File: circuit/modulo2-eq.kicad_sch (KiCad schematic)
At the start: 63 parts, among them J1 JACK_MONO, J2 HOLE, J3 HOLE, J4 CONN_01X04, J5 CONN_01X02, Q1 MMBFJ201, U1 NE5532, U2 NE5532, U3 NE5532, U4 NE5532, U5 TLE2426

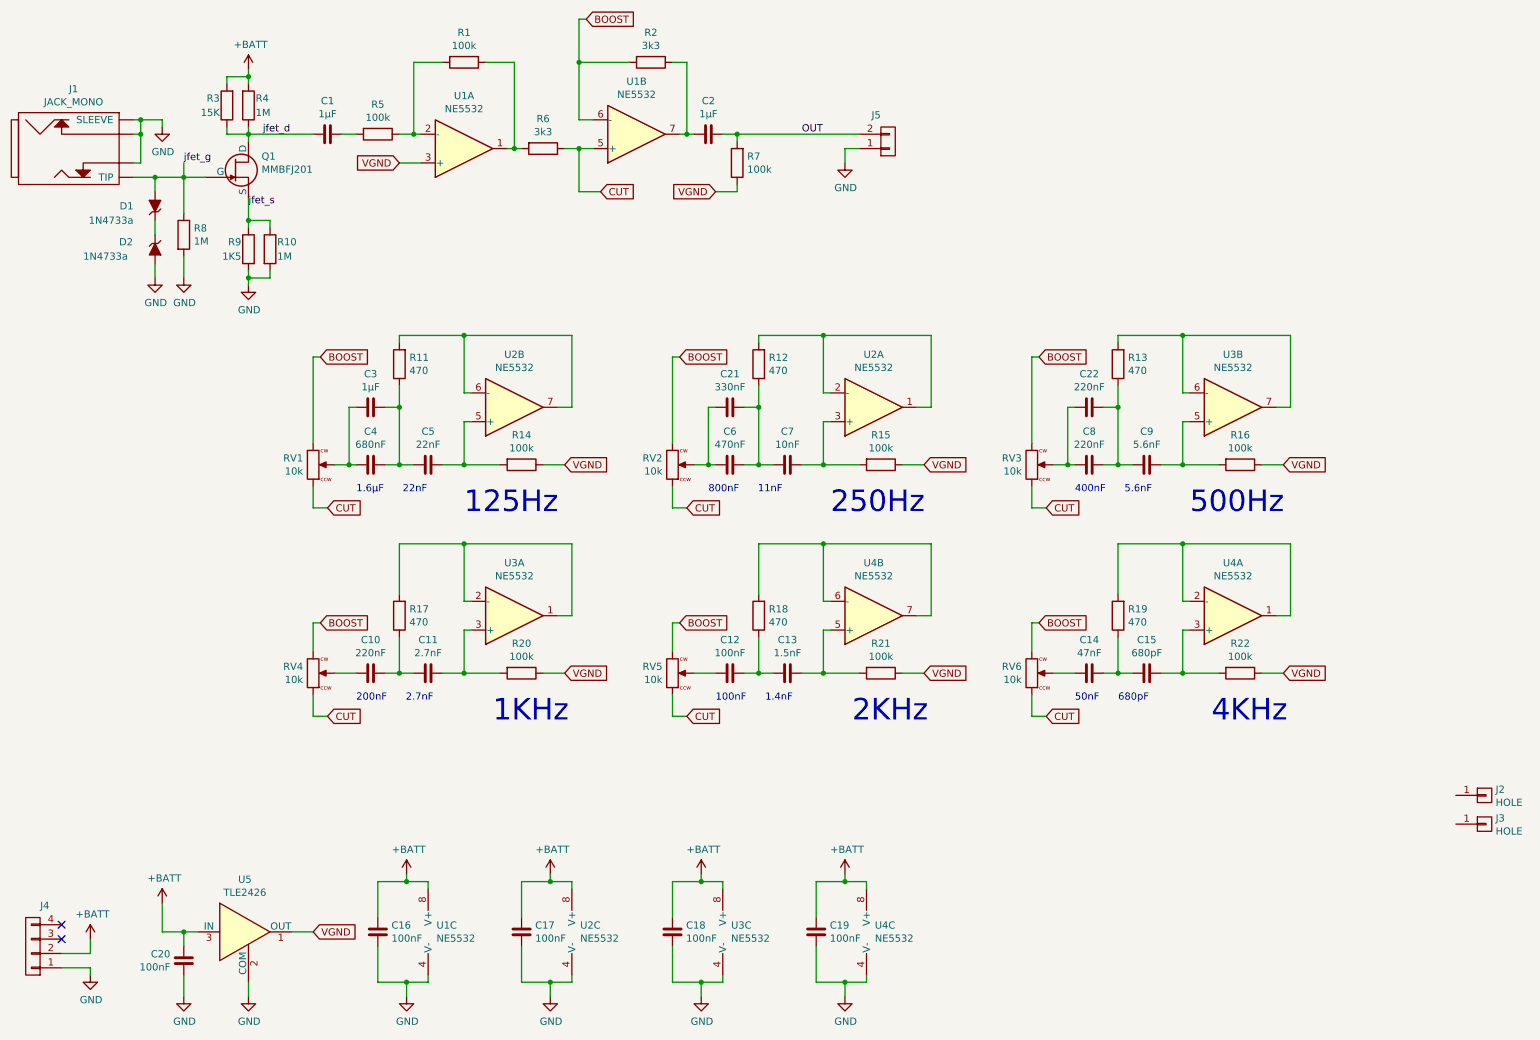
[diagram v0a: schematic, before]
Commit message: found new switch for gain select; eq needs redesign
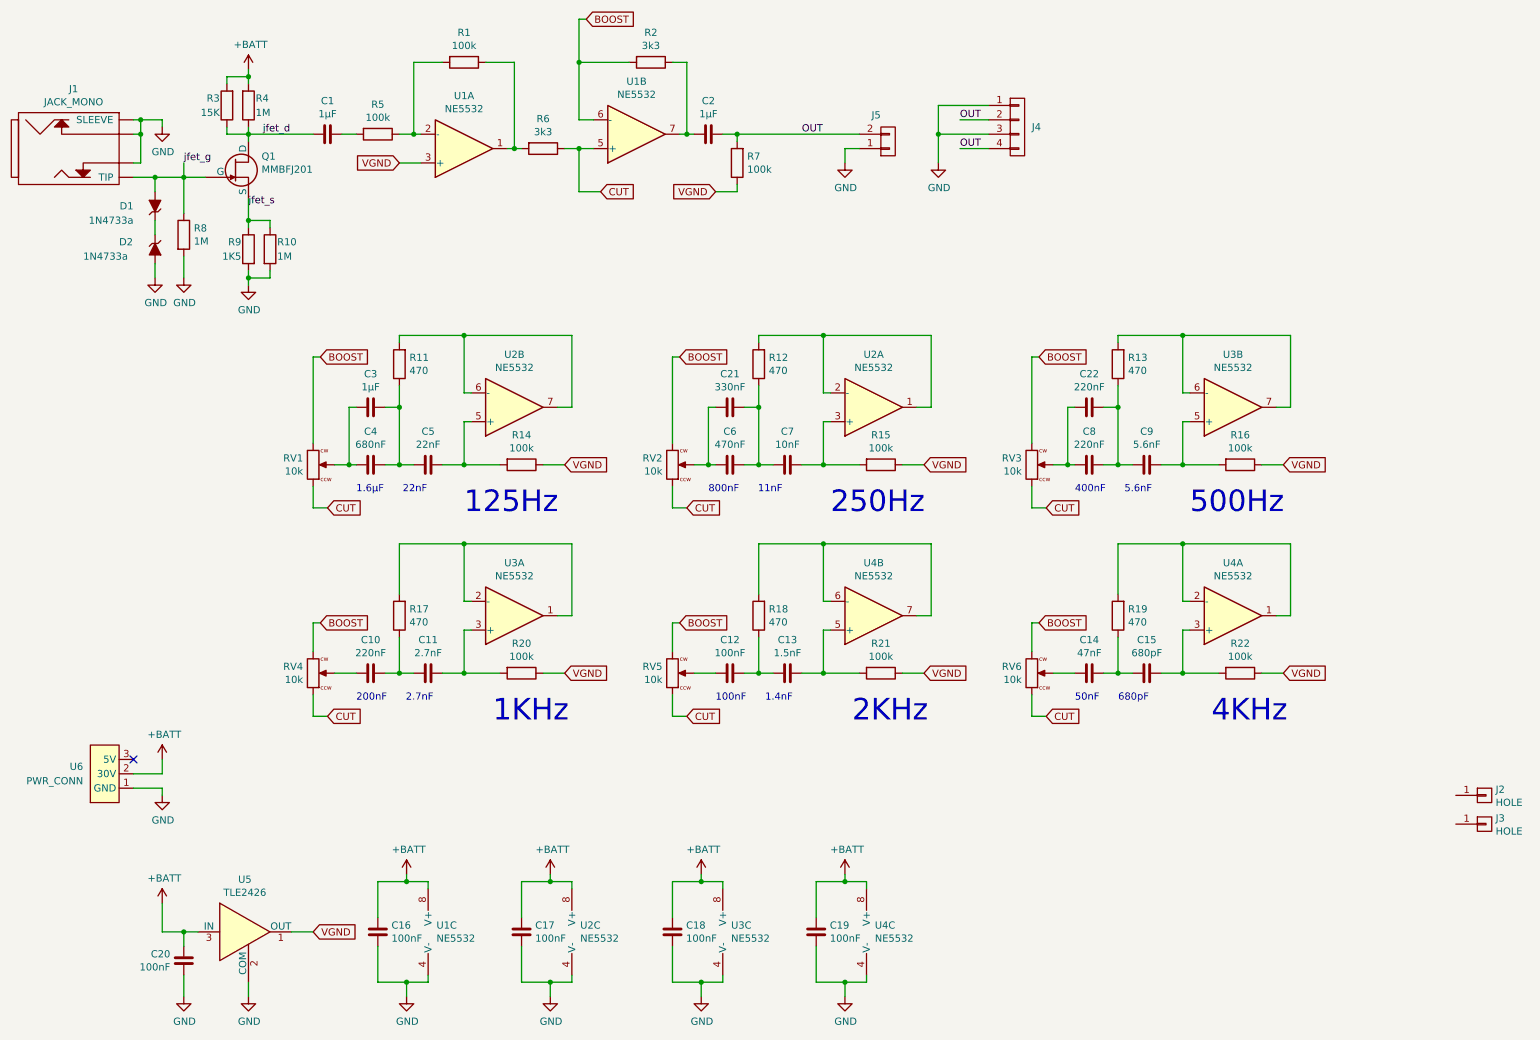
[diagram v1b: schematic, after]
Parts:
- added U6: PWR_CONN, myAmp:PWR_CONN, symbol myAmp:PWR_CONN
- R1, R10, R11, R12, R13, R14, R15, R16, R17, R18, R19, R2, R20, R21, R22, R3, R4, R5, R6, R7, R8, R9: footprint myAmp:R_10MM_TT -> myAmp:R_10MM
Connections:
- net +BATT: now also U6.2 (30V); no longer J4.2 (P2)
- net GND: now also J4.3, U6.1 (GND)
- net OUT: now also J4.2 (P2), J4.4
- no-connect marks 2 -> 1

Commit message: routed eq pcb
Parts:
- removed C2: 1μF, myAmp:C_5MM_1206, symbol myAmp:C
- removed R7: 100k, myAmp:R_10MM, symbol myAmp:R
- C1, C3: footprint myAmp:C_5MM_1206 -> myAmp:C_FILM_L7.2mm_W5.0mm_P5.00mm
- C10, C12, C8: footprint myAmp:C_5MM_1206 -> myAmp:C_FILM_L7.2mm_W3.5mm_P5.00mm
- C18: footprint myAmp:C_1206 -> myAmp:C_FILM_L7.2mm_W2.5mm_P5.00mm
- C21, C22, C4, C6: footprint myAmp:C_5MM_1206 -> myAmp:C_FILM_L7.2mm_W4.5mm_P5.00mm
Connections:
- net OUT: now also R2.1, U1.7
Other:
- moved on the sheet: J5
